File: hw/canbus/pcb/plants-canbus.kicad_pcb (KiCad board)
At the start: 2 copper layers, 75 x 27 mm, 21 parts, among them J1 Conn_01x02_Male, J2 Sensor, J3 Mini-DIN-6, J4 Mini-DIN-6, Q1 2N3904, Q2 S8550, Q3 2N3904, Q4 S8550, SW1 SW_Reset, U1 ATtiny85V-10P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

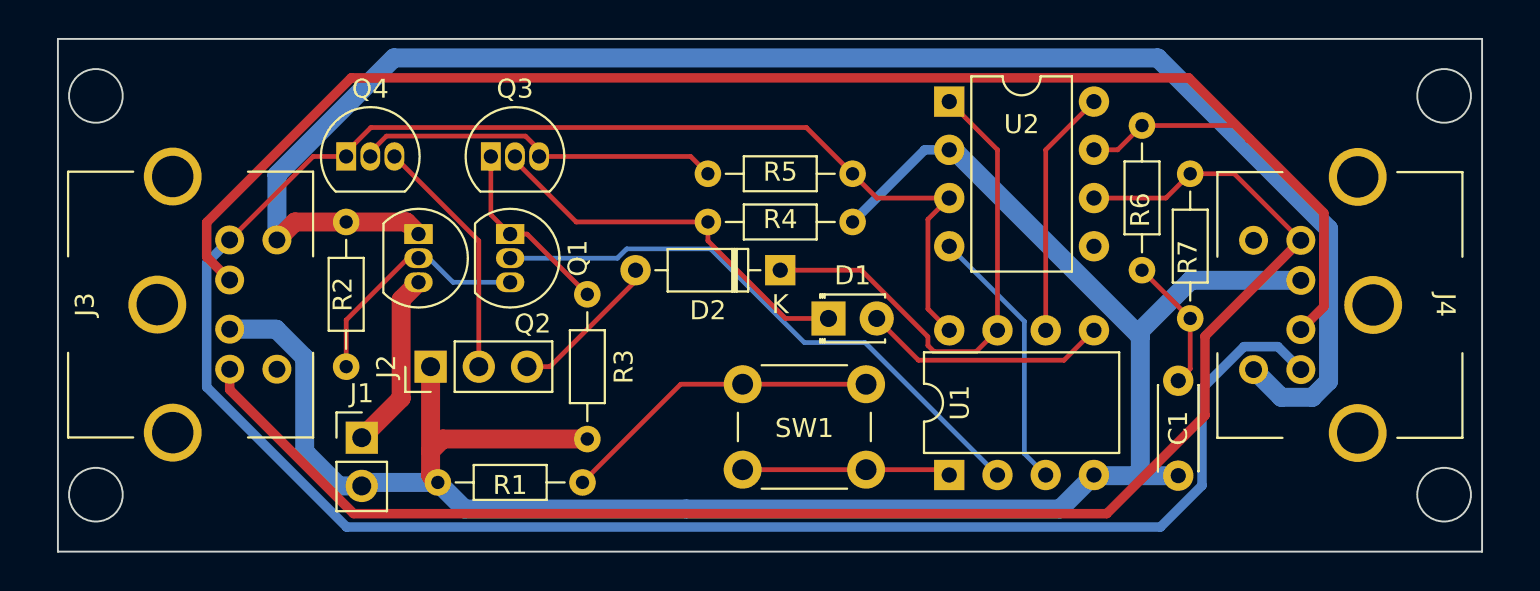
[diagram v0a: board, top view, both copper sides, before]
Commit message: Replace PS/2 connector with RJ12
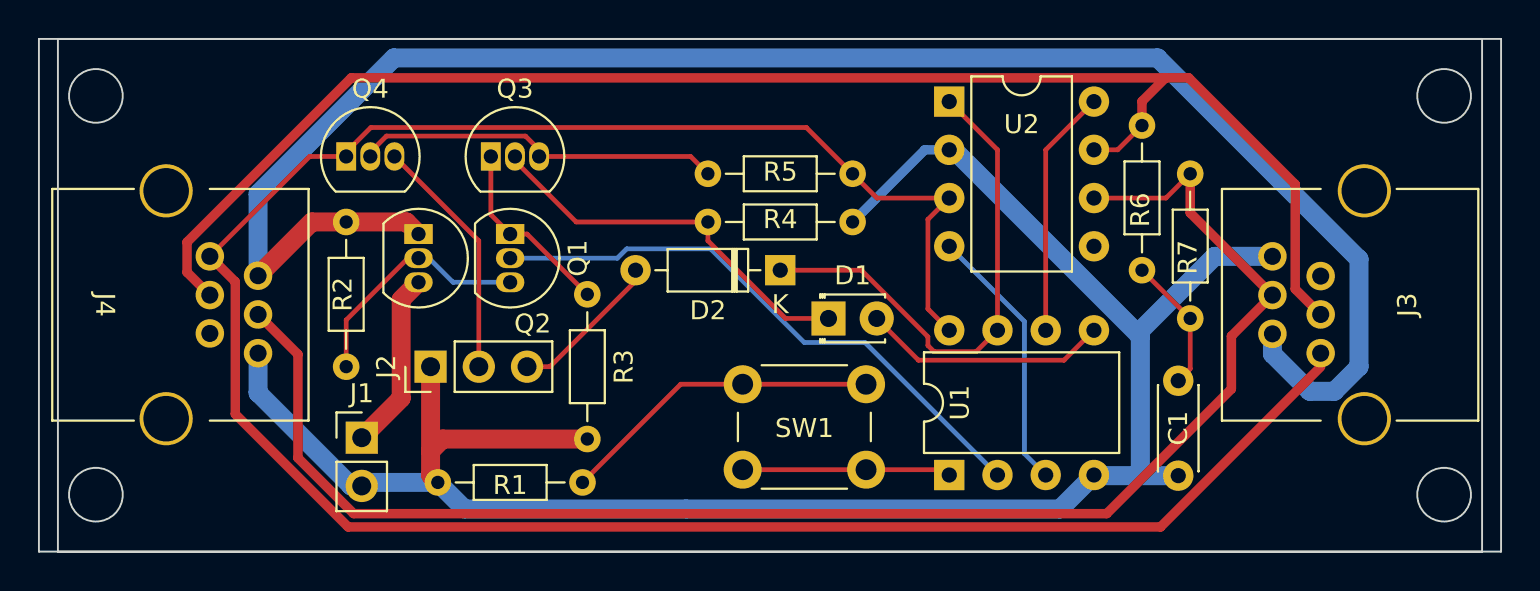
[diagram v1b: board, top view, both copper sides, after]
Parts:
- J3, J4: value Mini-DIN-6 -> 6P6C; footprint Footprints:Connector_MiniDIN_6 -> Footprints:RJ12_Pulse_E5566
- moved J3 61.3 mm to (94.5, 45.0)
- moved J4 61.3 mm to (36.0, 45.0)
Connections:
- J3 pad 2: CANH -> unconnected-(J3-Pad2)
- J3 pad 4: +5V -> CANH
- J3 pad 5: unconnected-(J3-Pad5) -> +12V
- J3 pad 6: +12V -> +5V
- J4 pad 2: CANH -> unconnected-(J4-Pad2)
- J4 pad 4: +5V -> CANH
- J4 pad 5: unconnected-(J4-Pad5) -> +12V
- J4 pad 6: +12V -> +5V
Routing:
- net +12V: track 86.1 -> 92.2 mm
- net GND: track 110.4 -> 105.8 mm
- net CANH: track 84.1 -> 81.0 mm
- net +5V: track 126.0 -> 123.1 mm
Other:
- board size 75 x 27 mm -> 77 x 27 mm
